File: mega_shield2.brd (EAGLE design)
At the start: 103.8 x 58.7 mm, 36 parts, among them IC1 L298, IC2 LM2937ET-5V, J2 Mega R3, M1_M2 1X2-3.5MM, M3_M4 1X2-3.5MM

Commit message: Minor changs to component placement
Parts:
- moved LED3 0.51 mm to (17.5, 26.7)
- moved LED4 0.51 mm to (17.5, 33.5)
- moved R4 0.51 mm to (17.5, 16.8)
- moved S1 0.25 mm to (12.2, 33.3)
- moved S2 0.25 mm to (22.9, 7.87)
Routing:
- net MOT1: track 78.8 -> 81.1 mm
- net MEGA_5V: track 95.2 -> 95.7 mm

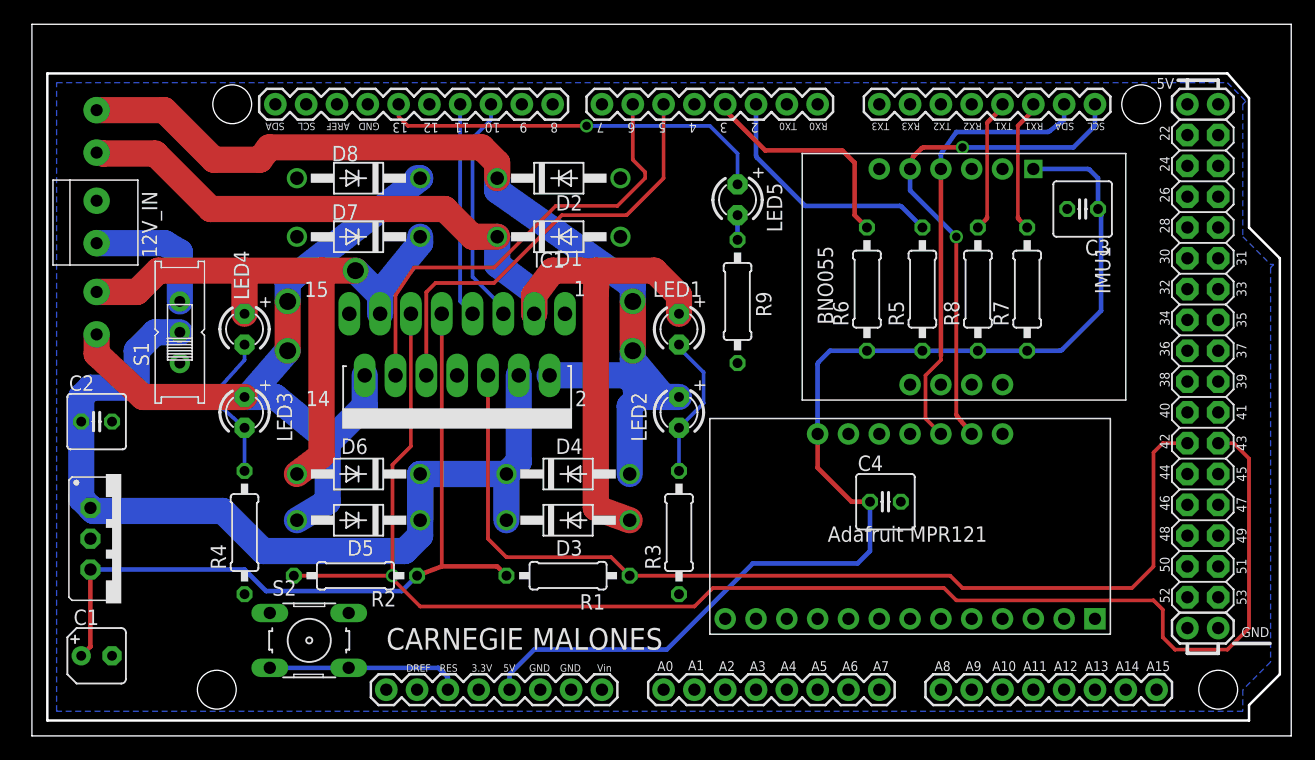
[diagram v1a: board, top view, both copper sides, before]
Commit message: Added 6 pin motor headers
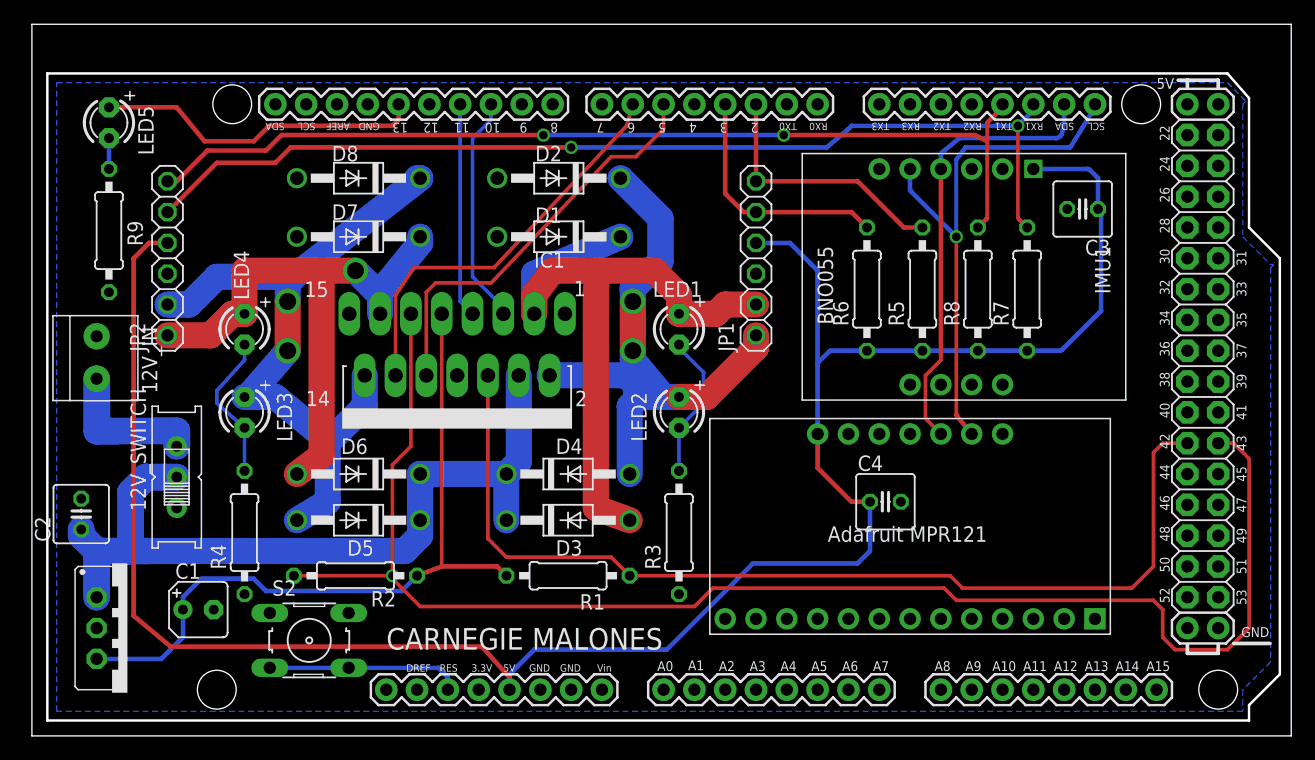
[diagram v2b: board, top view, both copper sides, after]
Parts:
- removed M1_M2, M3_M4: 1X2-3.5MM, adafruit:1X2-3.5MM
- removed S1: (no value), adafruit:EG1218
- added 12V_SWITCH: 12V_SWITCH, adafruit:EG1218
- added JP1: MOTOR1_HEADER, adafruit:1X06
- added JP2: MOTOR2_HEADER, adafruit:1X06
- moved LED5 52.2 mm to (6.35, 50.5)
- moved R9 52.1 mm to (6.35, 41.7)
- moved 12V_IN 11.2 mm to (5.33, 31.2)
- moved C1 9.21 mm to (13.7, 10.4)
- moved C2 7.73 mm to (4.06, 18.3), turned to 90 degrees
- moved IC2 7.38 mm to (5.33, 8.89)
- turned D1 to 180 degrees
- turned D2 to 180 degrees
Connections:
- removed net N$1: J2.2, R5.2
- removed net N$2: J2.3, R6.2
- new net MEGA2: J2.2, JP1.6, R5.2
- new net MEGA3: J2.3, JP1.5, R6.2
- net +12V: now also 12V_SWITCH.S; no longer S1.S
- net 12V_RAIL: now also 12V_SWITCH.P; no longer S1.P
- net GND: now also JP1.3, JP2.3
- net MEGA18: now also JP2.6
- net MEGA19: now also JP2.5
- net MEGA_5V: now also JP1.4, JP2.4
- net MOT1: now also JP1.1; no longer M1_M2.1
- net MOT2: now also JP1.2; no longer M1_M2.2
- net MOT3: now also JP2.1; no longer M3_M4.1
- net MOT4: now also JP2.2; no longer M3_M4.2
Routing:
- net MEGA_5V: track 95.7 -> 176.3 mm
- net MEGA19: track 11.0 -> 84.0 mm, vias 0 -> 2
- net MEGA18: track 11.0 -> 80.2 mm, vias 0 -> 2
- net MOT1: track 81.1 -> 49.9 mm
- net MOT2: track 83.3 -> 57.3 mm
- net MEGA2: track 0.00 -> 21.6 mm
- net N$1: track 20.4 -> 0.00 mm
- net MEGA3: track 0.00 -> 20.2 mm
- net N$2: track 18.7 -> 0.00 mm
- net 12V_RAIL: track 79.1 -> 71.0 mm
- net MOT3: track 53.8 -> 48.0 mm
- net N$3: track 32.8 -> 27.2 mm, vias 1 -> 0
- net MEGA6: track 38.0 -> 33.8 mm
- net MOT4: track 63.0 -> 59.1 mm
- net LDO_5V: track 64.3 -> 60.7 mm
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
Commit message: Added restricts to ground plane in brd file
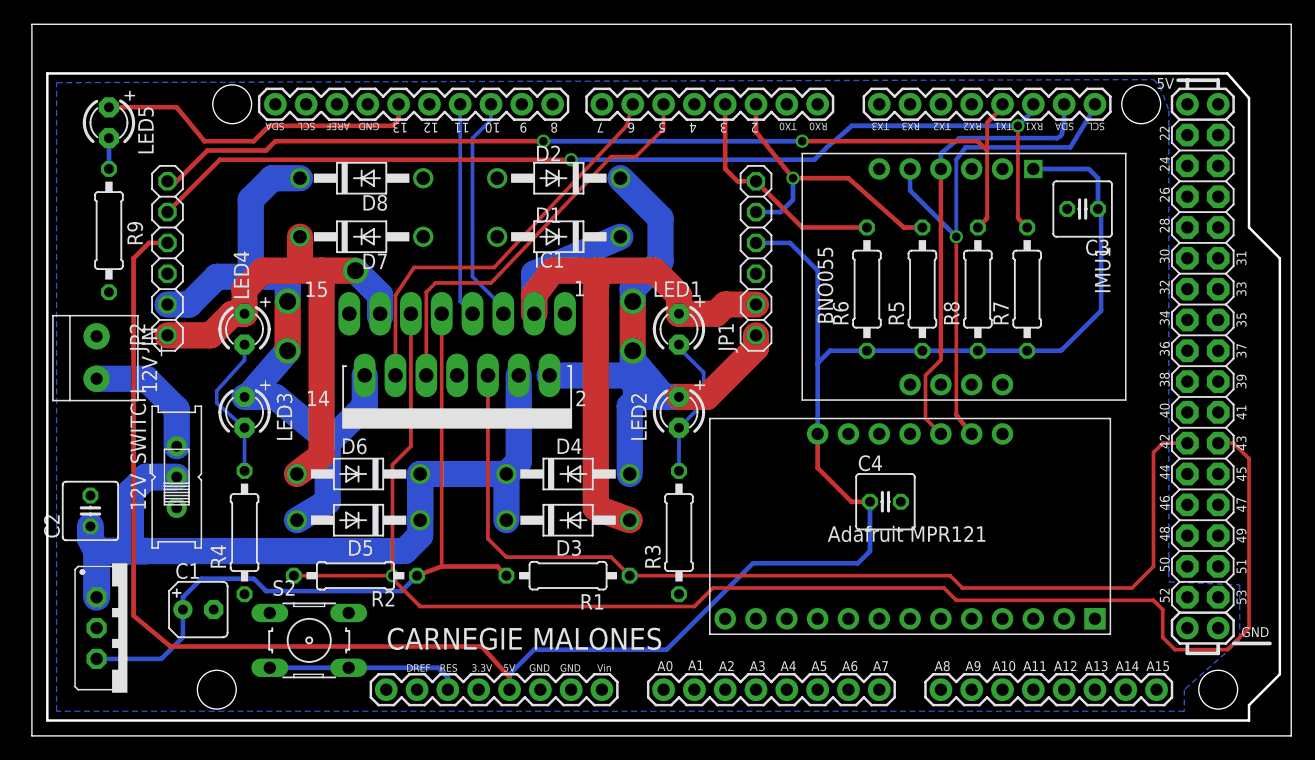
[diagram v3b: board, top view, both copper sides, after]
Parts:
- moved C2 0.80 mm to (4.83, 18.5)
- moved D7 0.25 mm to (27.2, 41.1), turned to 0 degrees
- moved D8 0.25 mm to (27.2, 46.0), turned to 0 degrees
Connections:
- net MEGA2: now also JP1.5; no longer JP1.6
- net MEGA3: now also JP1.6; no longer JP1.5
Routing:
- net MOT3: track 48.0 -> 44.3 mm
- net MOT4: track 59.1 -> 55.8 mm
- net MEGA2: track 21.6 -> 24.6 mm, vias 0 -> 1
- net +12V: track 12.2 -> 10.7 mm
- net MEGA3: track 20.2 -> 19.0 mm

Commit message: Added switch to library, shifted components around on brd
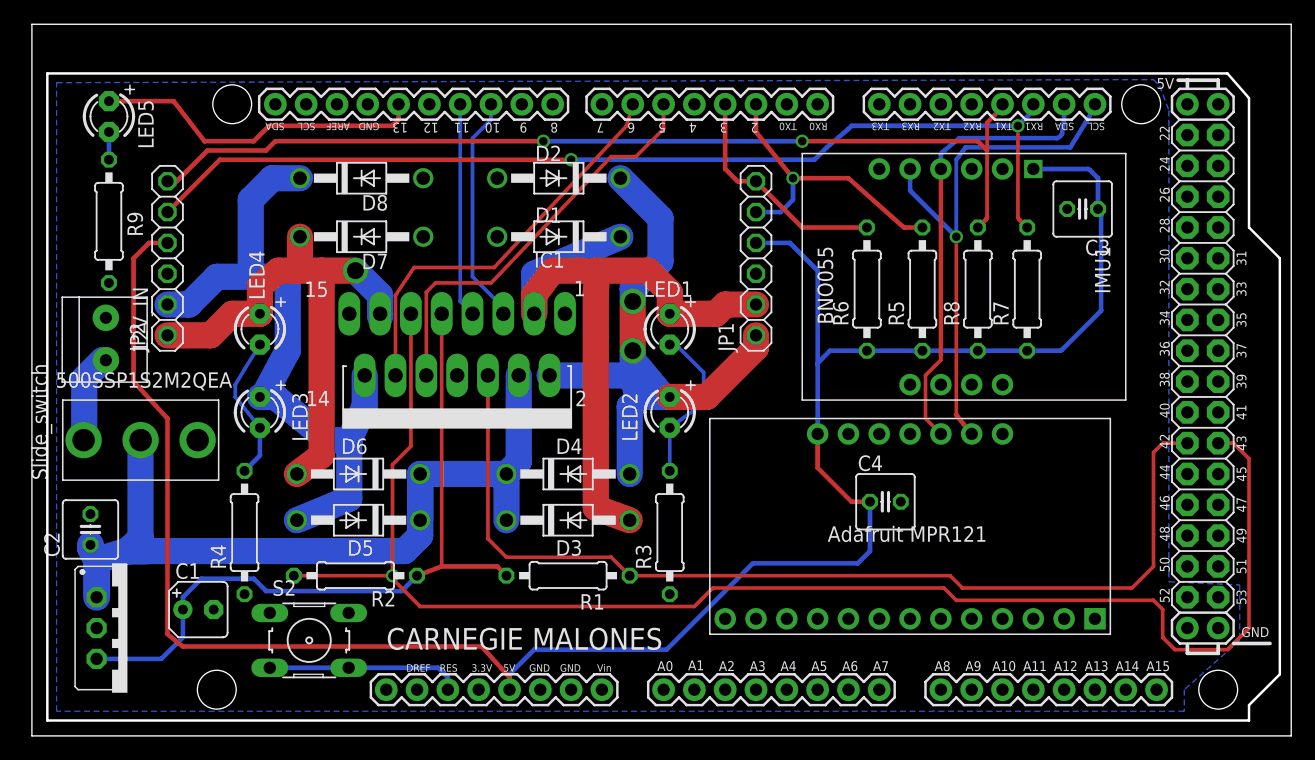
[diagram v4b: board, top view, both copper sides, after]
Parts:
- removed 12V_SWITCH: 12V_SWITCH, adafruit:EG1218
- added U$2: E-SWITCH_500SSP1S2M2QEA, arduinoShield:E-SWITCH_500SSP1S2M2QEA
- moved 12V_IN 1.70 mm to (6.10, 32.8)
- moved C2 1.52 mm to (4.83, 17.0)
- moved LED3 1.27 mm to (18.8, 26.7)
- moved LED4 1.27 mm to (18.8, 33.5)
- moved LED1 0.76 mm to (52.6, 33.5)
- moved LED2 0.76 mm to (52.6, 26.7)
- moved R3 0.76 mm to (52.6, 16.8)
- moved R9 0.76 mm to (6.35, 42.4)
- moved LED5 0.51 mm to (6.35, 51.1)
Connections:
- net +12V: now also U$2.L1; no longer 12V_SWITCH.S
- net 12V_RAIL: now also U$2.COM; no longer 12V_SWITCH.P
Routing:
- net +12V: track 10.7 -> 7.51 mm
- net N$7: track 12.1 -> 13.2 mm
- net 12V_RAIL: track 70.8 -> 69.7 mm
- net MEGA_5V: track 176.3 -> 175.6 mm
- net MOT4: vias 2 -> 0

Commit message: added excel component list, changed resistor values
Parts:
- R3, R4: value 1.8K -> 2.2K
- R9: value 330 -> 390
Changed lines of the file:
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@@
 <attribute name="VALUE" x="24.4094" y="12.573" size="1.27" layer="27" ratio="10"/>
 </element>
-<element name="R3" library="rcl" package="0207/10" value="1.8K" x="52.578" y="16.764" rot="R90"/>
-<element name="R4" library="rcl" package="0207/10" value="1.8K" x="17.526" y="16.764" rot="R90"/>
+<element name="R3" library="rcl" package="0207/10" value="2.2K" x="52.578" y="16.764" rot="R90"/>
+<element name="R4" library="rcl" package="0207/10" value="2.2K" x="17.526" y="16.764" rot="R90"/>
 <element name="R5" library="rcl" package="0207/10" value="1K" x="73.406" y="36.83" rot="R90"/>
 <element name="R6" library="rcl" package="0207/10" value="1K" x="68.834" y="36.83" rot="R90"/>
 <element name="R7" library="rcl" package="0207/10" value="1K" x="82.042" y="36.83" rot="R90"/>
 <element name="R8" library="rcl" package="0207/10" value="1K" x="77.978" y="36.83" rot="R90"/>
-<element name="R9" library="rcl" package="0207/10" value="330" x="6.35" y="42.418" smashed="yes" rot="R90">
+<element name="R9" library="rcl" package="0207/10" value="390" x="6.35" y="42.418" smashed="yes" rot="R90">
 <attribute name="NAME" x="9.144" y="41.148" size="1.27" layer="25" ratio="10" rot="R90"/>
 <attribute name="VALUE" x="6.985" y="40.6654" size="1.27" layer="27" ratio="10" rot="R90"/>

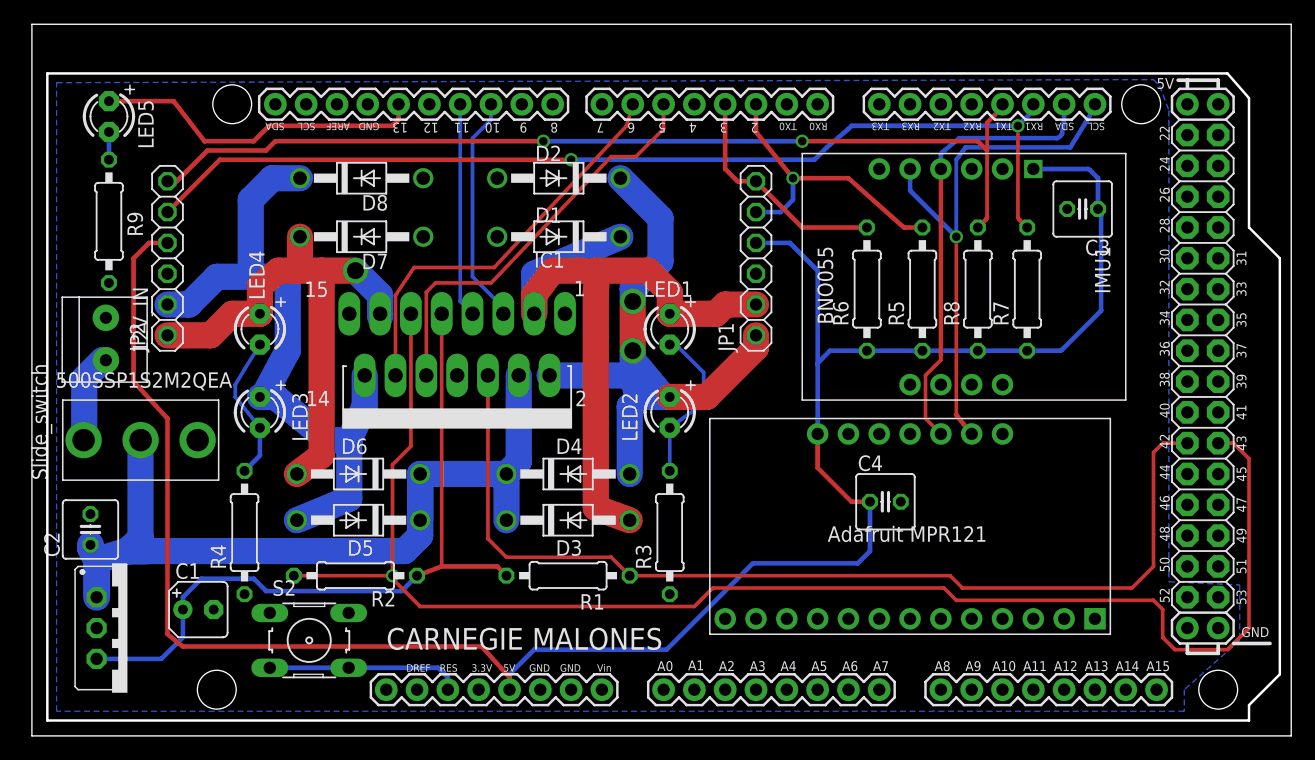
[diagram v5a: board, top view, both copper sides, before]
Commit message: changes to silkscreen
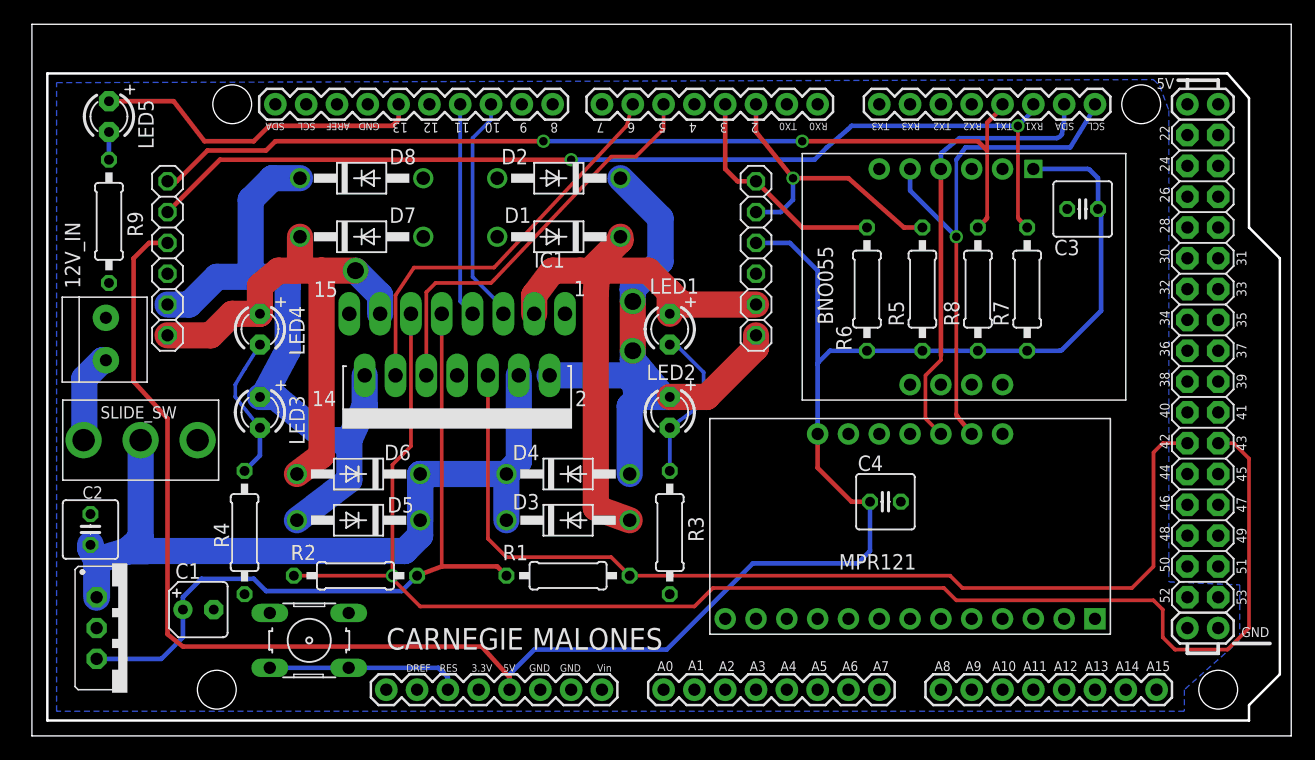
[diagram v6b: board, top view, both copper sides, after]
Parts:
- removed U$2: E-SWITCH_500SSP1S2M2QEA, arduinoShield:E-SWITCH_500SSP1S2M2QEA
- added SLIDE_SW: E-SWITCH_500SSP1S2M2QEA, arduinoShield:E-SWITCH_500SSP1S2M2QEA
- JP1: value MOTOR1_HEADER -> MOTOR_1
- JP2: value MOTOR2_HEADER -> MOTOR_2
- renumbered U$1 to MPR121
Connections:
- net +12V: now also SLIDE_SW.L1; no longer U$2.L1
- net 12V_RAIL: now also SLIDE_SW.COM; no longer U$2.COM
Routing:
- net MOT2: track 57.4 -> 50.4 mm
- net MOT4: track 55.8 -> 55.1 mm

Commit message: shifted some components around, edited silkscreen
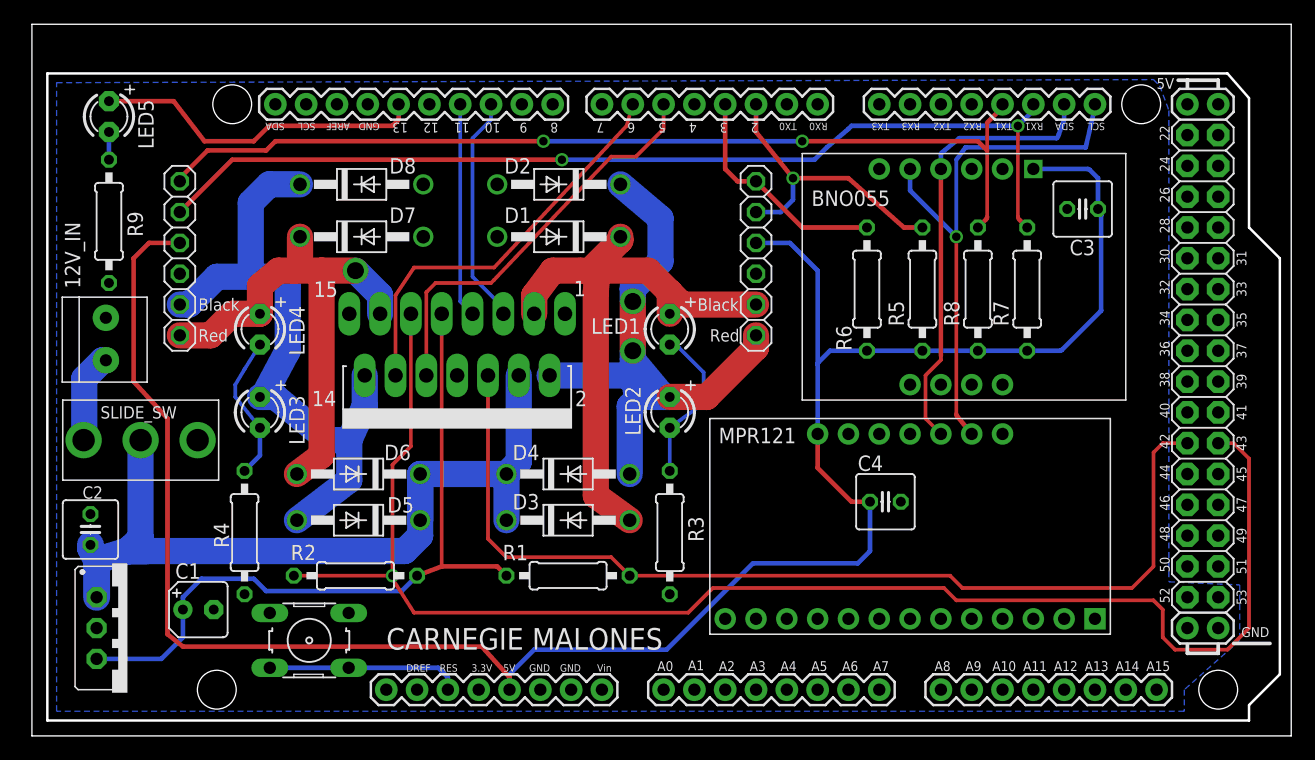
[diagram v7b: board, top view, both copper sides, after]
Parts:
- moved JP2 1.02 mm to (12.2, 39.4)
- moved D2 0.51 mm to (43.4, 45.5)
- moved D8 0.51 mm to (27.2, 45.5)
- renumbered IMU1 to BNO055
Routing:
- net MOT4: track 55.1 -> 53.7 mm
- net MEGA_5V: track 175.6 -> 176.6 mm
- net MEGA19: track 84.0 -> 83.0 mm
- net MOT3: track 44.2 -> 43.1 mm
- net MEGA43: track 124.0 -> 124.8 mm
- net MEGASCL: track 44.3 -> 45.0 mm
- net MOT2: track 50.4 -> 49.9 mm
- net MEGA18: track 80.2 -> 79.7 mm
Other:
- board text added: "Black"
- board text added: "Red"
